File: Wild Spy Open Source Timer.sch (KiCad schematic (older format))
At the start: 41 parts, among them Q1 AO3415, Q2 AO3415, Q3 AO3415, Q4 AO3415, Q5 AO3415, Q6 AO3415, SW1 SW_PUSH, SW2 ORD213, U1 DS3232SN, U2 TPS70933DBVR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

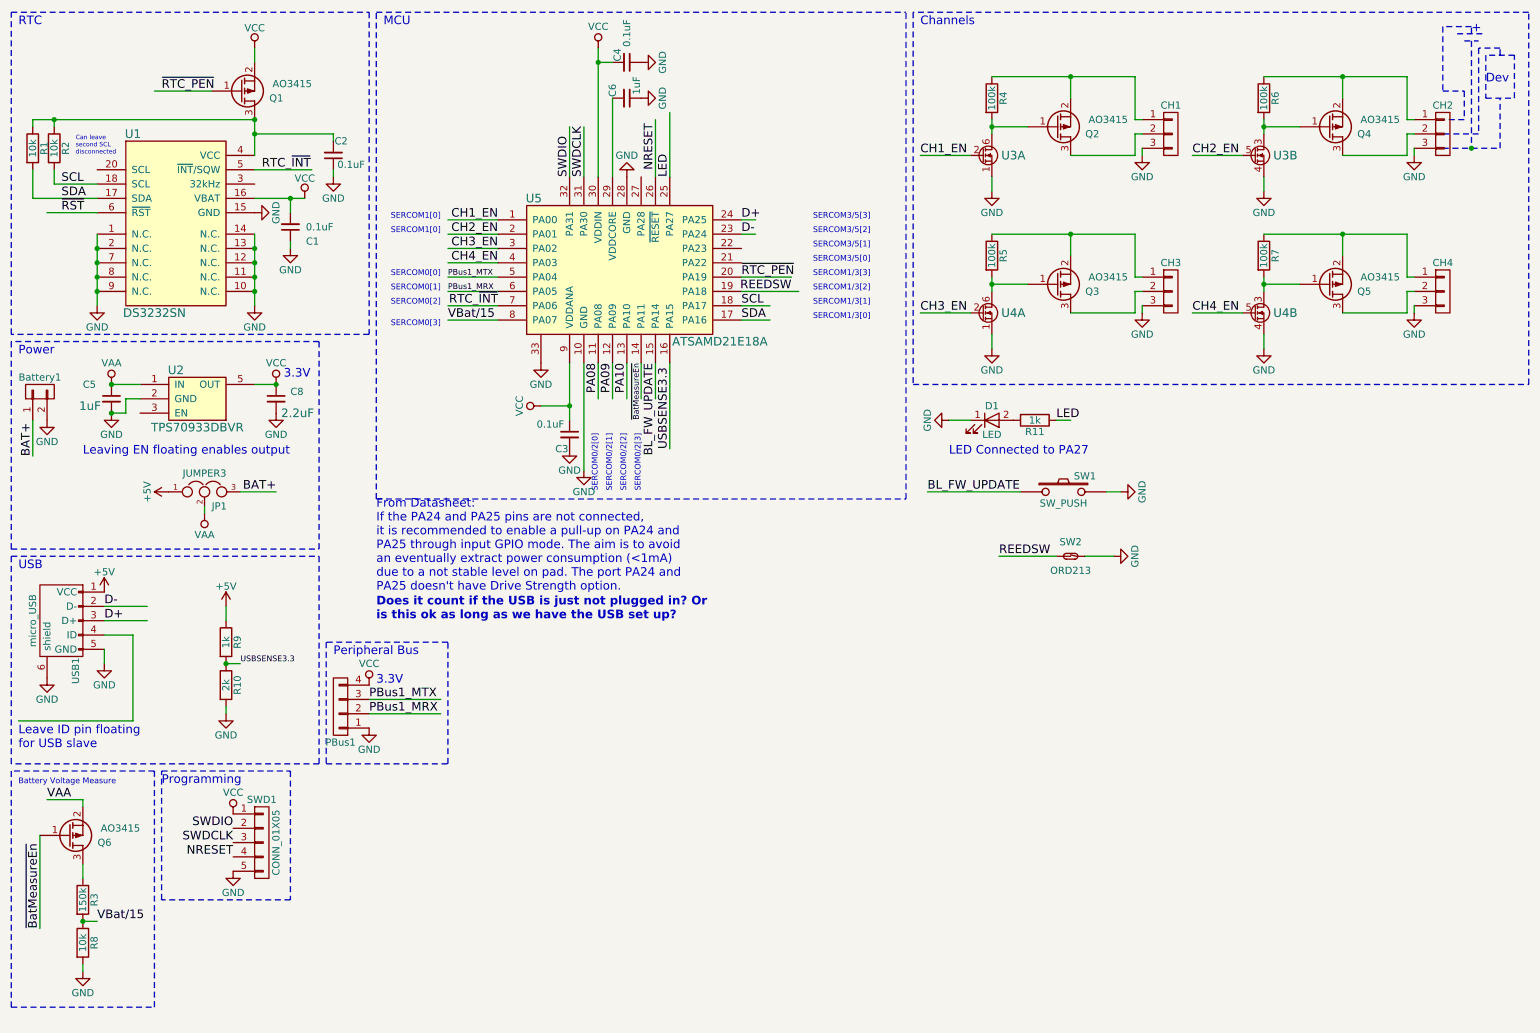
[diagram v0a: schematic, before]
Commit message: Fixed battery volrage measurement issue in hardware.
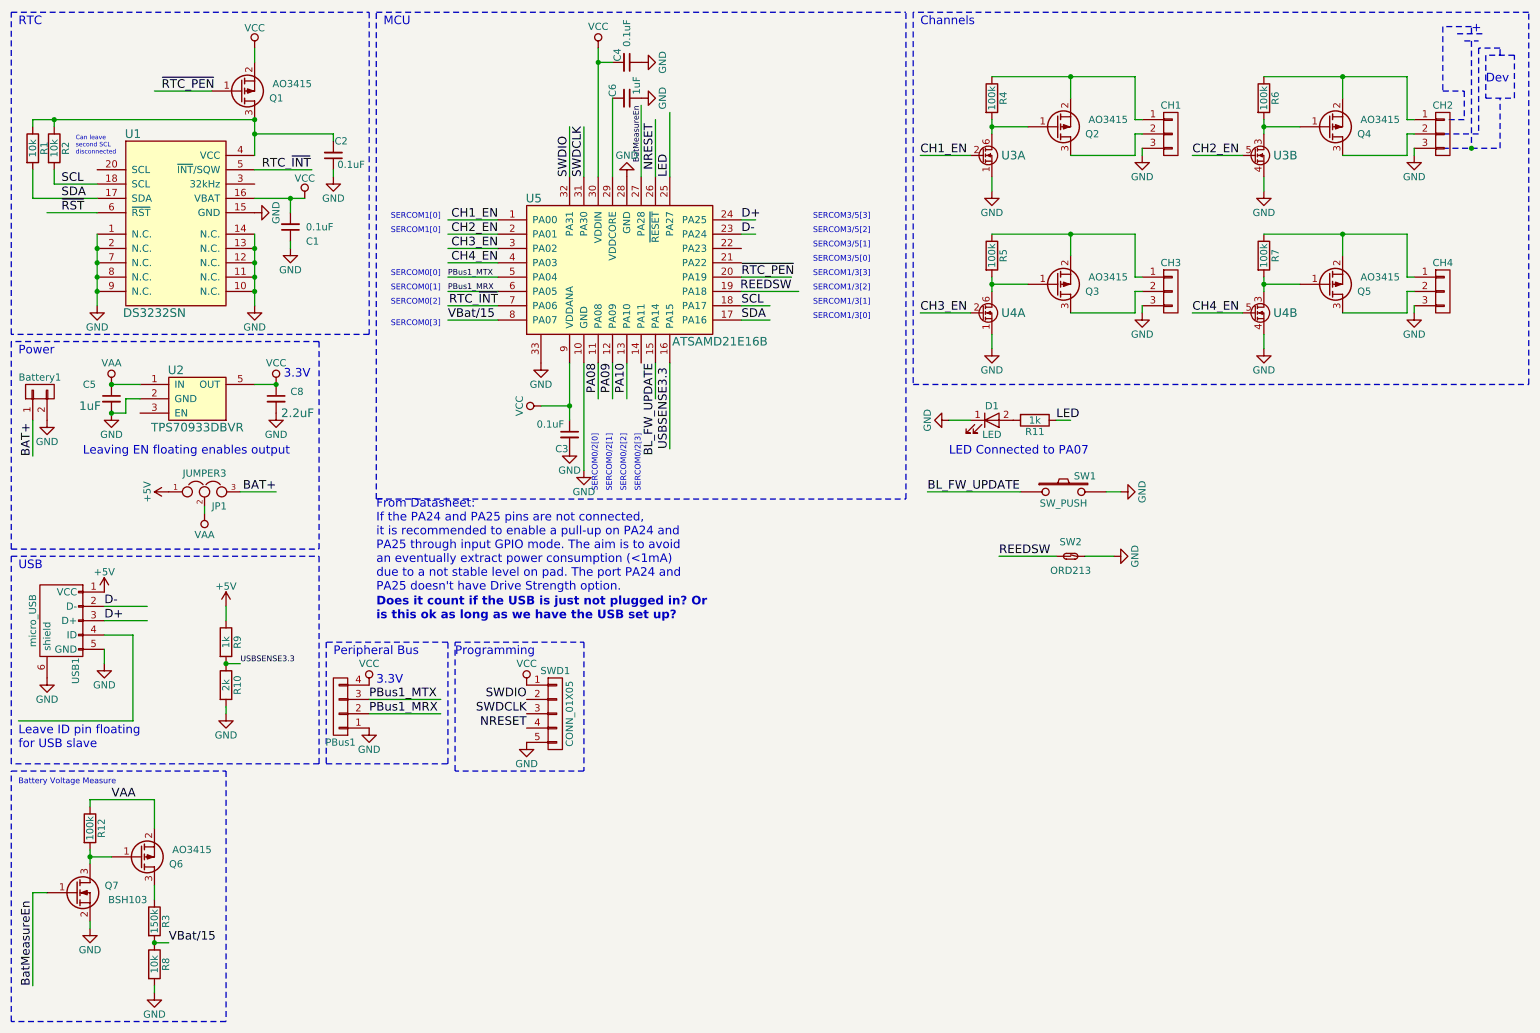
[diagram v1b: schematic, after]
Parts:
- added Q7: BSH103, OSTFootprints:SOT-23-HandSoldering, symbol Q_NMOS_GSD
- added R12: 100k, Resistors_SMD:R_0603_HandSoldering, symbol R
- U5: value ATSAMD21E18A -> ATSAMD21E16B
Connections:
- net labels added: BatMeasureEn
- net labels removed: ~BatMeasureEn
- wire segments 129 -> 134
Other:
- note added: "LED Connected to PA07\n"
- note removed: "LED Connected to PA27\n"
- moved on the sheet: Q6, R3, R8, SWD1
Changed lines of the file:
@@
 L CONN_01X05 SWD1
 U 1 1 590A49F4
-P 2300 6350
-F 0 "SWD1" H 2300 6650 50  0000 C CNN
-F 1 "CONN_01X05" V 2400 6350 50  0000 C CNN
-F 2 "OSTFootprints:SWD_PROG_HEADER_L" H 2300 6350 50  0001 C CNN
-F 3 "" H 2300 6350 50  0001 C CNN
-F 4 "dnf" H 2300 6350 60  0001 C CNN "fit_field"
-	1    2300 6350
+P 4350 5450
+F 0 "SWD1" H 4350 5750 50  0000 C CNN
+F 1 "CONN_01X05" V 4450 5450 50  0000 C CNN
+F 2 "OSTFootprints:SWD_PROG_HEADER_L" H 4350 5450 50  0001 C CNN
+F 3 "" H 4350 5450 50  0001 C CNN
+F 4 "dnf" H 4350 5450 60  0001 C CNN "fit_field"
+	1    4350 5450
 	1    0    0    -1
 $EndComp
@@
 L VCC #PWR034
 U 1 1 590A4E37
-P 2100 6150
-F 0 "#PWR034" H 2100 6000 50  0001 C CNN
-F 1 "VCC" H 2100 6300 50  0000 C CNN
-F 2 "" H 2100 6150 50  0000 C CNN
-F 3 "" H 2100 6150 50  0000 C CNN
-	1    2100 6150
+P 4150 5250
+F 0 "#PWR034" H 4150 5100 50  0001 C CNN
+F 1 "VCC" H 4150 5400 50  0000 C CNN
+F 2 "" H 4150 5250 50  0000 C CNN
+F 3 "" H 4150 5250 50  0000 C CNN
+	1    4150 5250
 	1    0    0    -1
 $EndComp
 Text Label 5050 1650 1    60   ~ 0
 NRESET
-Text Label 2100 6450 2    60   ~ 0
+Text Label 4150 5550 2    60   ~ 0
 NRESET
 $Comp
 L GND #PWR035
 U 1 1 590A6395
-P 2100 6550
-F 0 "#PWR035" H 2100 6300 50  0001 C CNN
-F 1 "GND" H 2100 6400 50  0000 C CNN
-F 2 "" H 2100 6550 50  0000 C CNN
-F 3 "" H 2100 6550 50  0000 C CNN
-	1    2100 6550
+P 4150 5650
+F 0 "#PWR035" H 4150 5400 50  0001 C CNN
+F 1 "GND" H 4150 5500 50  0000 C CNN
+F 2 "" H 4150 5650 50  0000 C CNN
+F 3 "" H 4150 5650 50  0000 C CNN
+	1    4150 5650
 	1    0    0    -1
 $EndComp
@@
 Text Label 4550 1700 1    60   ~ 0
 SWDCLK
-Text Label 2100 6250 2    60   ~ 0
+Text Label 4150 5350 2    60   ~ 0
 SWDIO
-Text Label 2100 6350 2    60   ~ 0
+Text Label 4150 5450 2    60   ~ 0
 SWDCLK
 Text Label 4850 3000 3    60   ~ 0
 PA10
-Text Notes 1600 5950 0    60   ~ 0
+Text Notes 3650 5050 0    60   ~ 0
 Programming
 Text Notes 600  4450 0    60   ~ 0
@@
 L R R3
 U 1 1 5911D863
-P 1050 6750
-F 0 "R3" V 1130 6750 50  0000 C CNN
-F 1 "150k" V 1050 6750 50  0000 C CNN
-F 2 "Resistors_SMD:R_0603_HandSoldering" V 980 6750 50  0001 C CNN
-F 3 "" H 1050 6750 50  0000 C CNN
-F 4 "5%" V 1050 6750 60  0001 C CNN "Accuracy"
-	1    1050 6750
+P 1550 6900
+F 0 "R3" V 1630 6900 50  0000 C CNN
+F 1 "150k" V 1550 6900 50  0000 C CNN
+F 2 "Resistors_SMD:R_0603_HandSoldering" V 1480 6900 50  0001 C CNN
+F 3 "" H 1550 6900 50  0000 C CNN
+F 4 "5%" V 1550 6900 60  0001 C CNN "Accuracy"
+	1    1550 6900
 	1    0    0    -1
 $EndComp
@@
 L R R8
 U 1 1 5911D869
-P 1050 7050
-F 0 "R8" V 1130 7050 50  0000 C CNN
-F 1 "10k" V 1050 7050 50  0000 C CNN
-F 2 "Resistors_SMD:R_0603_HandSoldering" V 980 7050 50  0001 C CNN
-F 3 "" H 1050 7050 50  0000 C CNN
-F 4 "5%" V 1050 7050 60  0001 C CNN "Accuracy"
-	1    1050 7050
+P 1550 7200
+F 0 "R8" V 1630 7200 50  0000 C CNN
+F 1 "10k" V 1550 7200 50  0000 C CNN
+F 2 "Resistors_SMD:R_0603_HandSoldering" V 1480 7200 50  0001 C CNN
+F 3 "" H 1550 7200 50  0000 C CNN
+F 4 "5%" V 1550 7200 60  0001 C CNN "Accuracy"
+	1    1550 7200
 	1    0    0    -1
 $EndComp
@@
 L GND #PWR037
 U 1 1 5911D86F
-P 1050 7250
-F 0 "#PWR037" H 1050 7000 50  0001 C CNN
-F 1 "GND" H 1050 7100 50  0000 C CNN
-F 2 "" H 1050 7250 50  0000 C CNN
-F 3 "" H 1050 7250 50  0000 C CNN
-	1    1050 7250
-	1    0    0    -1
-$EndComp
-Text Label 1150 6900 0    60   ~ 0
+P 1550 7400
+F 0 "#PWR037" H 1550 7150 50  0001 C CNN
+F 1 "GND" H 1550 7250 50  0000 C CNN
+F 2 "" H 1550 7400 50  0000 C CNN
+F 3 "" H 1550 7400 50  0000 C CNN
+	1    1550 7400
+	1    0    0    -1
+$EndComp
+Text Label 1650 7050 0    60   ~ 0
 VBat/15
 $Comp
 L Q_PMOS_GSD Q6
 U 1 1 591226FE
-P 950 6300
-F 0 "Q6" H 1250 6350 50  0000 R CNN
-F 1 "AO3415" H 1450 6250 50  0000 R CNN
-F 2 "OSTFootprints:SOT-23-HandSoldering" H 1150 6400 50  0001 C CNN
-F 3 "http://aosmd.com/res/data_sheets/AO3415.pdf" H 950 6300 50  0001 C CNN
-F 4 "-20V" H 950 6300 60  0001 C CNN "Vdss"
-F 5 "53mOhm" H 950 6300 60  0001 C CNN "Rds(on)"
-F 6 "785-1010-2-ND" H 950 6300 60  0001 C CNN "Supplier 1 Part Number"
-F 7 "DigiKey" H 950 6300 60  0001 C CNN "Supplier 1"
-F 8 "0.11771" H 950 6300 60  0001 C CNN "Supplier 1 Cost"
-F 9 "AUD" H 950 6300 60  0001 C CNN "Supplier 1 Currency"
-	1    950  6300
+P 1450 6450
+F 0 "Q6" H 1750 6500 50  0000 R CNN
+F 1 "AO3415" H 1950 6400 50  0000 R CNN
+F 2 "OSTFootprints:SOT-23-HandSoldering" H 1650 6550 50  0001 C CNN
+F 3 "http://aosmd.com/res/data_sheets/AO3415.pdf" H 1450 6450 50  0001 C CNN
+F 4 "-20V" H 1450 6450 60  0001 C CNN "Vdss"
+F 5 "53mOhm" H 1450 6450 60  0001 C CNN "Rds(on)"
+F 6 "785-1010-2-ND" H 1450 6450 60  0001 C CNN "Supplier 1 Part Number"
+F 7 "DigiKey" H 1450 6450 60  0001 C CNN "Supplier 1"
+F 8 "0.11771" H 1450 6450 60  0001 C CNN "Supplier 1 Cost"
+F 9 "AUD" H 1450 6450 60  0001 C CNN "Supplier 1 Currency"
+	1    1450 6450
 	1    0    0    1
 $EndComp
-Text Label 800  6050 0    60   ~ 0
+Text Label 1250 6050 0    60   ~ 0
 VAA
 Text Label 700  3650 1    60   ~ 0
@@
 Text Label 2400 3900 2    60   ~ 0
 BAT+
-Text Label 750  6950 1    60   ~ 0
-~BatMeasureEn
+Text Label 700  7350 1    60   ~ 0
+BatMeasureEn
 Text Label 3600 2700 0    60   ~ 0
 VBat/15
-Text Label 4950 3000 3    40   ~ 0
-~BatMeasureEn
+Text Label 4950 1200 3    40   ~ 0
+BatMeasureEn
 Text Label 3050 5350 0    60   ~ 0
 PBus1_MTX
@@
 	4650 800  4650 1700
 Wire Notes Line
-	2500 5850 2500 6750
-Wire Notes Line
-	2500 6750 1600 6750
-Wire Notes Line
-	1600 6750 1600 5850
-Wire Notes Line
-	1600 5850 2500 5850
+	4550 4950 4550 5850
+Wire Notes Line
+	4550 5850 3650 5850
+Wire Notes Line
+	3650 5850 3650 4950
+Wire Notes Line
+	3650 4950 4550 4950
 Wire Notes Line
 	550  4350 2700 4350
@@
 	4850 3250 4850 3000
 Wire Wire Line
-	4950 3250 4950 3000
-Wire Wire Line
 	5050 3250 5050 3000
 Wire Wire Line
 	5150 3000 5150 3600
 Wire Wire Line
-	1150 6900 1050 6900
-Wire Wire Line
-	1050 7250 1050 7200
-Connection ~ 1050 6900
-Wire Wire Line
-	1050 6500 1050 6600
-Wire Wire Line
-	1050 6050 1050 6100
-Wire Wire Line
-	1050 6050 800  6050
+	1650 7050 1550 7050
+Wire Wire Line
+	1550 7400 1550 7350
+Connection ~ 1550 7050
+Wire Wire Line
+	1550 6650 1550 6750
+Wire Wire Line
+	1550 6050 1550 6250
 Wire Wire Line
 	5150 1700 5150 1250
@@
 Wire Wire Line
 	3050 5450 3550 5450
-Wire Wire Line
-	750  6300 750  6950
-Wire Notes Line
-	550  5850 550  7500
-Wire Notes Line
-	550  7500 1550 7500
-Wire Notes Line
-	1550 7500 1550 5850
-Wire Notes Line
-	1550 5850 550  5850
 Wire Wire Line
 	4450 3000 4450 3400
@@
 LED
 Text Notes 7100 3650 0    60   ~ 0
-LED Connected to PA27\n
+LED Connected to PA07\n
 Wire Wire Line
 	7100 3400 7250 3400
@@
 P 4750 2400
 F 0 "U5" H 4200 2950 60  0000 C CNN
-F 1 "ATSAMD21E18A" H 5500 1950 60  0000 C CNN
+F 1 "ATSAMD21E16B" H 5500 1950 60  0000 C CNN
 F 2 "OSTFootprints:QFN-32-1EP_5x5mm_Pitch0.5mm" H 4100 2850 60  0001 C CNN
 F 3 "http://www.atmel.com/Images/Atmel-42181-SAM-D21_Datasheet.pdf" H 4200 2950 60  0001 C CNN
@@
 $EndComp
 Connection ~ 4450 3300
+$Comp
+L Q_NMOS_GSD Q7
+U 1 1 59882BA0
+P 1000 6700
+F 0 "Q7" H 1300 6750 50  0000 R CNN
+F 1 "BSH103" H 1500 6650 50  0000 R CNN
+F 2 "OSTFootprints:SOT-23-HandSoldering" H 1200 6800 50  0001 C CNN
+F 3 "https://assets.nexperia.com/documents/data-sheet/BSH103.pdf" H 1000 6700 50  0001 C CNN
+F 4 "1727-4319-1-ND" H 1000 6700 60  0001 C CNN "Supplier 1 Part Number"
+F 5 "Digikey" H 1000 6700 60  0001 C CNN "Supplier 1"
+F 6 "0.419" H 1000 6700 60  0001 C CNN "Supplier 1 Cost"
+F 7 "AUD" H 1000 6700 60  0001 C CNN "Supplier 1 Currency"
+	1    1000 6700
+	1    0    0    -1
+$EndComp
+$Comp
+L R R12
+U 1 1 59884DBA
+P 1100 6250
+F 0 "R12" V 1180 6250 50  0000 C CNN
+F 1 "100k" V 1100 6250 50  0000 C CNN
+F 2 "Resistors_SMD:R_0603_HandSoldering" V 1030 6250 50  0001 C CNN
+F 3 "" H 1100 6250 50  0000 C CNN
+	1    1100 6250
+	1    0    0    -1
+$EndComp
+Wire Wire Line
+	1550 6050 1100 6050
+Wire Wire Line
+	1100 6050 1100 6100
+Wire Wire Line
+	1100 6400 1100 6500
+Wire Wire Line
+	1100 6450 1250 6450
+Connection ~ 1100 6450
+$Comp
+L GND #PWR044
+U 1 1 598858A4
+P 1100 6950
+F 0 "#PWR044" H 1100 6700 50  0001 C CNN
+F 1 "GND" H 1100 6800 50  0000 C CNN
+F 2 "" H 1100 6950 50  0000 C CNN
+F 3 "" H 1100 6950 50  0000 C CNN
+	1    1100 6950
+	1    0    0    -1
+$EndComp
+Wire Wire Line
+	1100 6950 1100 6900
+Wire Wire Line
+	700  6700 700  7350
+Wire Wire Line
+	700  6700 800  6700
+Wire Notes Line
+	550  5850 2050 5850
+Wire Notes Line
+	2050 5850 2050 7600
+Wire Notes Line
+	2050 7600 550  7600
+Wire Notes Line
+	550  7600 550  5850
+Wire Wire Line
+	4950 1700 4950 1200
 $EndSCHEMATC

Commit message: Manufacturing outputs for Rev1.1
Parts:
- C1, C2, C3, C4: Supplier 1 (none) -> DigiKey; Supplier 1 Cost (none) -> 0.0062; Supplier 1 Currency (none) -> AUD; Supplier 1 Part Number (none) -> 1276-1011-1-ND
- C6: Supplier 1 (none) -> DigiKey; Supplier 1 Cost (none) -> 0.018; Supplier 1 Currency (none) -> AUD; Supplier 1 Part Number (none) -> 1276-1182-1-ND
- C8: Supplier 1 Cost 0.0337 -> 0.0356
- D1: Supplier 1 (none) -> DigiKey; Supplier 1 Cost (none) -> 0.13080; Supplier 1 Currency (none) -> AUD; Supplier 1 Part Number (none) -> 475-2512-1-ND
- R1, R2: Accuracy (none) -> 5%; Supplier 1 (none) -> DigiKey; Supplier 1 Cost (none) -> 0.006; Supplier 1 Currency (none) -> AUD; Supplier 1 Part Number (none) -> 311-10KGRCT-ND
- R10: Accuracy (none) -> 5%; Supplier 1 (none) -> DigiKey; Supplier 1 Cost (none) -> 0.006; Supplier 1 Currency (none) -> AUD; Supplier 1 Part Number (none) -> 311-2.0KGRCT-ND
- R11, R9: Accuracy (none) -> 5%; Supplier 1 (none) -> DigiKey; Supplier 1 Cost (none) -> 0.006; Supplier 1 Currency (none) -> AUD; Supplier 1 Part Number (none) -> 311-1.0KGRCT-ND
- R3: Supplier 1 (none) -> DigiKey; Supplier 1 Cost (none) -> 0.006; Supplier 1 Currency (none) -> AUD; Supplier 1 Part Number (none) -> 311-150KGRCT-ND
- R4, R5, R6, R7: Supplier 1 (none) -> DigiKey; Supplier 1 Cost (none) -> 0.006; Supplier 1 Currency (none) -> AUD; Supplier 1 Part Number (none) -> 311-100KGRCT-ND
- R8: Supplier 1 (none) -> DigiKey; Supplier 1 Cost (none) -> 0.006; Supplier 1 Currency (none) -> AUD; Supplier 1 Part Number (none) -> 311-10KGRCT-ND
- SW2: Supplier 1 Cost (none) -> 2.07; Supplier 1 Currency (none) -> AUD; Supplier 1 Part Number (none) -> 374-1087-ND; Supplier Cost 1 2.07 -> (none); Supplier Currency 1 AUD -> (none); Supplier Part Number 1 374-1087-ND -> (none)
- U3, U4: Supplier 1 Cost $0.08638 -> 0.08638
- U5: Supplier 1 Cost (none) -> 3.014; Supplier 1 Currency (none) -> AUD
